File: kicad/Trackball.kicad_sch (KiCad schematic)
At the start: 40 parts, among them J1 Conn_01x04, J2 Conn_02x10_Odd_Even, SW1 SW_Push, SW2 SW_Push, U1 TCR2EF19, U2 PMW3360, U3 RP2040, U4 TLV73333PDBV, U5 W25Q128JVS, Y1 Crystal_GND24

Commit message: up
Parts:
- removed C1, C17, C2, C3, C4, C5, C6, C7, C8, C9: 100n, Capacitor_SMD:C_0402_1005Metric, symbol Device:C_Small
- removed C10, C13: 1u, Capacitor_SMD:C_0402_1005Metric, symbol Device:C_Small
- removed C18, C19: 30p, Capacitor_SMD:C_0402_1005Metric, symbol Device:C_Small
- removed J2: Conn_02x10_Odd_Even, Connector_PinHeader_2.54mm:PinHeader_2x10_P2.54mm_Vertical, symbol Connector_Generic:Conn_02x10_Odd_Even
- removed R3, R4: 27, Resistor_SMD:R_0402_1005Metric, symbol Device:R_Small
- removed R5: 10k, Resistor_SMD:R_0402_1005Metric, symbol Device:R_Small
- removed R6, R7: 1k, Resistor_SMD:R_0402_1005Metric, symbol Device:R_Small
- removed SW1, SW2: SW_Push, Button_Switch_SMD:SW_SPST_Omron_B3FS-100xP, symbol Switch:SW_Push
- removed U3: RP2040, RP2040:RP2040-QFN-56, symbol RP2040:RP2040
- removed U5: W25Q128JVS, Package_SO:SOIC-8_5.23x5.23mm_P1.27mm, symbol Trackball-rescue:W25Q128JVS-Memory_Flash
- removed Y1: Crystal_GND24, Crystal:Crystal_SMD_3225-4Pin_3.2x2.5mm, symbol Device:Crystal_GND24
- added C101, C102, C108, C110: 0.1u, Capacitor_SMD:C_0805_2012Metric, symbol Device:C_Small
- added C109, C111: 1u, Capacitor_SMD:C_0805_2012Metric, symbol Device:C_Small
- added J101: Conn_02x03_Counter_Clockwise, Connector_Harwin:Harwin_Gecko-G125-FVX0605L0X_2x03_P1.25mm_Vertical, symbol Connector_Generic:Conn_02x03_Counter_Clockwise
- added R103, R104: 10k, Resistor_SMD:R_0805_2012Metric, symbol Device:R_Small
- added SW1, SW2: Push_Button, PCM_Switch_Keyboard_Hotswap_Kailh:SW_Hotswap_Kailh_Choc_V1V2_1.00u, symbol PCM_SL_Devices:Push_Button
- added SW102: Push_Button, PCM_4ms_Switch:Switch_Toggle_SPDT_SubMini, symbol Switch:SW_Wuerth_450301014042
- added SW103, SW106: Push_Button, Button_Switch_SMD:SW_Push_1P1T_NO_CK_KSC7xxJ, symbol PCM_SL_Devices:Push_Button
- added SW3: RotaryEncoder_Switch_MP, PMW3360:RollerEncoder_Panasonic_EVQWGD001, symbol Device:RotaryEncoder_Switch_MP
- added U7: ESP32-S3-WROOM-2, PCM_Espressif:ESP32-S3-WROOM-2, symbol PCM_Espressif:ESP32-S3-WROOM-2
- C103: renamed from C15; footprint Capacitor_SMD:C_0402_1005Metric -> Capacitor_SMD:C_0805_2012Metric
- C104: renamed from C14; footprint Capacitor_SMD:C_0402_1005Metric -> Capacitor_SMD:C_0805_2012Metric
- C105: renamed from C16; footprint Capacitor_SMD:C_0402_1005Metric -> Capacitor_SMD:C_0805_2012Metric
- C106: renamed from C11; footprint Capacitor_SMD:C_0603_1608Metric -> Capacitor_SMD:C_0805_2012Metric
- C107: renamed from C12; footprint Capacitor_SMD:C_0603_1608Metric -> Capacitor_SMD:C_0805_2012Metric
- R101: renamed from R1; footprint Resistor_SMD:R_0402_1005Metric -> Resistor_SMD:R_0805_2012Metric
- R102: renamed from R2; footprint Resistor_SMD:R_0402_1005Metric -> Resistor_SMD:R_0805_2012Metric
- renumbered U1 to U103
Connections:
- net +3V3: now also J101.6 (Pin_6), R103.1, R104.1, SW102.2 (C), U7.2 (3V3)
- net +5V: now also SW102.3 (A); no longer C106.2, U103.1 (IN), U103.3 (EN)
- net D+: now also U7.14 (GPIO20/U1CTS/ADC2_CH9/CLK_OUT1/USB_D+)
- net D-: now also U7.13 (GPIO19/U1RTS/ADC2_CH8/CLK_OUT2/USB_D-)
- net GND: now also C101.2, C102.1, C108.1, C109.2, C110.1, C111.2, J101.5 (Pin_5), SW1.1, SW103.2, SW106.2, SW2.1, SW3.C, SW3.MP, SW3.S2, U7.1 (GND), U7.40 (GND), U7.41 (GND)
- net GPIO16: now also U7.9 (GPIO16/U0CTS/ADC2_CH5/XTAL_32K_N)
- net GPIO17: now also U7.10 (GPIO17/U1TXD/ADC2_CH6)
- net GPIO18: now also U7.11 (GPIO18/U1RXD/ADC2_CH7/CLK_OUT3)
- net MISO: now also U7.34 (MTDI/GPIO41/CLK_OUT1)
- net MOSI: now also U7.33 (MTDO/GPIO40/CLK_OUT2)
- net MOTION: now also U7.38 (GPIO2/TOUCH2/ADC1_CH1)
- net NCS: now also U7.35 (MTMS/GPIO42)
- net SCLK: now also U7.32 (MTCK/GPIO39/CLK_OUT3/SUBSPICS1)
- new net: C106.2, SW102.1 (B), U103.1 (IN), U103.3 (EN)
- new net EN: C108.2, C109.1, J101.1 (Pin_1), R103.2, SW103.1, U7.3 (EN)
- new net GPIO0: C110.2, C111.1, J101.4 (Pin_4), R104.2, SW106.1, U7.27 (GPIO0/BOOT)
- new net GPIO09: C102.2, SW3.B, U7.17 (GPIO9/TOUCH9/ADC1_CH8/FSPIHD/SUBSPIHD)
- new net GPIO10: C101.1, SW3.A, U7.18 (GPIO10/TOUCH10/ADC1_CH9/FSPICS0/FSPIIO4/SUBSPICS0)
- new net GPIO3: SW2.2, U7.15 (GPIO3/TOUCH3/ADC1_CH2)
- new net GPIO38: SW3.S1, U7.31 (GPIO38/FSPIWP/SUBSPIWP)
- new net GPIO46: SW1.2, U7.16 (GPIO46)
- new net RX: J101.3 (Pin_3), U7.36 (U0RXD/GPIO44/CLK_OUT2)
- new net TX: J101.2 (Pin_2), U7.37 (U0TXD/GPIO43/CLK_OUT1)
- no-connect marks 3 -> 1
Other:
- note removed: "Crystal"
- note removed: "Flash"
- note removed: "GPIO"

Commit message: update
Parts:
- added Brd101: SSD1306, SSD1306:128x64OLED, symbol SSD1306-128x64_OLED:SSD1306
- added D101, D102: LED_3mm, LED_THT:LED_D3.0mm, symbol PCM_SL_Devices:LED_3mm
- added R105, R106: R_1206, PCM_4ms_Resistor:R_0805_2012Metric, symbol PCM_Resistor_AKL:R_1206
- added SW101, SW104: Push_Button, PCM_openinput:SW_Micro_Switch, symbol PCM_SL_Devices:Push_Button
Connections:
- net +3V3: now also Brd101.2 (VCC)
- net GND: now also Brd101.1 (GND), D101.1, D102.1, SW101.1, SW104.1
- net GPIO25: now also SW1.2, U7.25 (GPIO48/SPICLK_N/SUBSPICLK_N_DIFF), SW101.2
- net GPIO3: now also R106.2; no longer SW2.2
- net GPIO38: now also R105.2; no longer SW3.S1
- net GPIO46: now also SW2.2, SW104.2; no longer SW1.2
- net MISO: now also U7.33 (MTDO/GPIO40/CLK_OUT2); no longer U7.34 (MTDI/GPIO41/CLK_OUT1)
- net MOSI: now also U7.34 (MTDI/GPIO41/CLK_OUT1); no longer U7.33 (MTDO/GPIO40/CLK_OUT2)
- net NCS: now also U7.32 (MTCK/GPIO39/CLK_OUT3/SUBSPICS1); no longer U7.35 (MTMS/GPIO42)
- net SCLK: now also U7.35 (MTMS/GPIO42); no longer U7.32 (MTCK/GPIO39/CLK_OUT3/SUBSPICS1)
- net GPIO11: now reaches U7.19 (GPIO11/TOUCH11/ADC2_CH0/FSPID/FSPIIO5/SUBSPID)
- net GPIO11: now also Brd101.4 (SDA)
- net GPIO12: now reaches U7.20 (GPIO12/TOUCH12/ADC2_CH1/FSPICLK/FSPIIO6/SUBSPICLK)
- net GPIO12: now also Brd101.3 (SCL)
- net GPIO13: now reaches U7.21 (GPIO13/TOUCH13/ADC2_CH2/FSPIQ/FSPIIO7/SUBSPIQ)
- net GPIO14: now reaches U7.22 (GPIO14/TOUCH14/ADC2_CH3/FSPIWP/FSPIDQS/SUBSPIWP)
- net GPIO14: now also SW3.S1
- net GPIO21: now reaches U7.23 (GPIO21)
- net GPIO21: now also C101.1, SW3.A
- net GPIO37: now reaches U7.24 (GPIO47/SPICLK_P/SUBSPICLK_P_DIFF)
- net GPIO37: now also C102.2, SW3.B
- removed net GPIO09: C102.2, SW3.B, U7.17 (GPIO9/TOUCH9/ADC1_CH8/FSPIHD/SUBSPIHD)
- removed net GPIO10: C101.1, SW3.A, U7.18 (GPIO10/TOUCH10/ADC1_CH9/FSPICS0/FSPIIO4/SUBSPICS0)
- new net: D101.2, R105.1
- new net: D102.2, R106.1
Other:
- moved on the sheet: SW2

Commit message: V1 prebuild
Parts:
- added J2: Conn_02x04_Counter_Clockwise, Connector_IDC:IDC-Header_2x04_P2.54mm_Vertical, symbol Connector_Generic:Conn_02x04_Counter_Clockwise
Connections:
- net +3V3: now also J2.2 (Pin_2)
- net GND: now also J2.1 (Pin_1)
- net GPIO13: now also J2.3 (Pin_3)
- net GPIO18: now also J2.6 (Pin_6)
- net GPIO8: now reaches U7.12 (GPIO8/TOUCH8/ADC1_CH7/SUBSPICS1)
- net GPIO8: now also J2.4 (Pin_4)
- net GPIO9: now reaches U7.17 (GPIO9/TOUCH9/ADC1_CH8/FSPIHD/SUBSPIHD)
- net GPIO9: now also J2.8 (Pin_8)
- net GPIO10: now reaches U7.18 (GPIO10/TOUCH10/ADC1_CH9/FSPICS0/FSPIIO4/SUBSPICS0)
- net GPIO10: now also J2.5 (Pin_5)
- net GPIO45: now reaches U7.26 (GPIO45)
- net GPIO45: now also J2.7 (Pin_7)

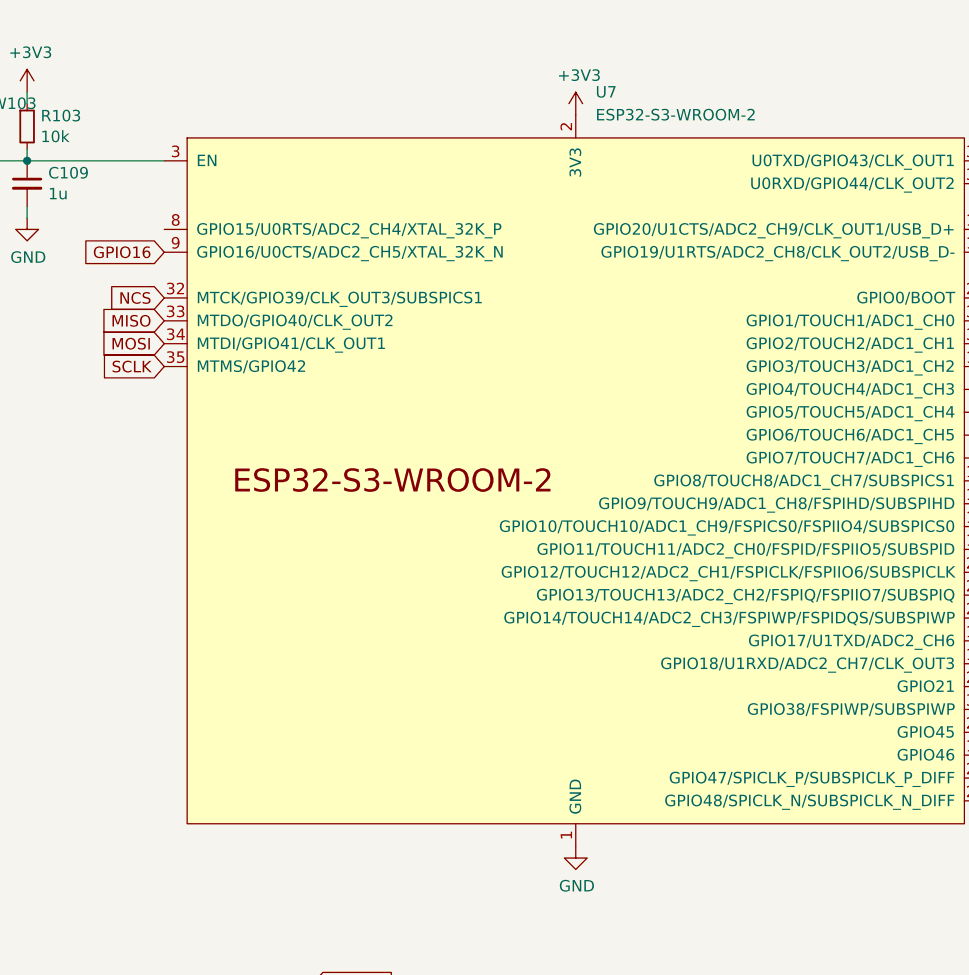
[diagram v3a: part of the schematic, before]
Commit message: changement wroom 2 a 1
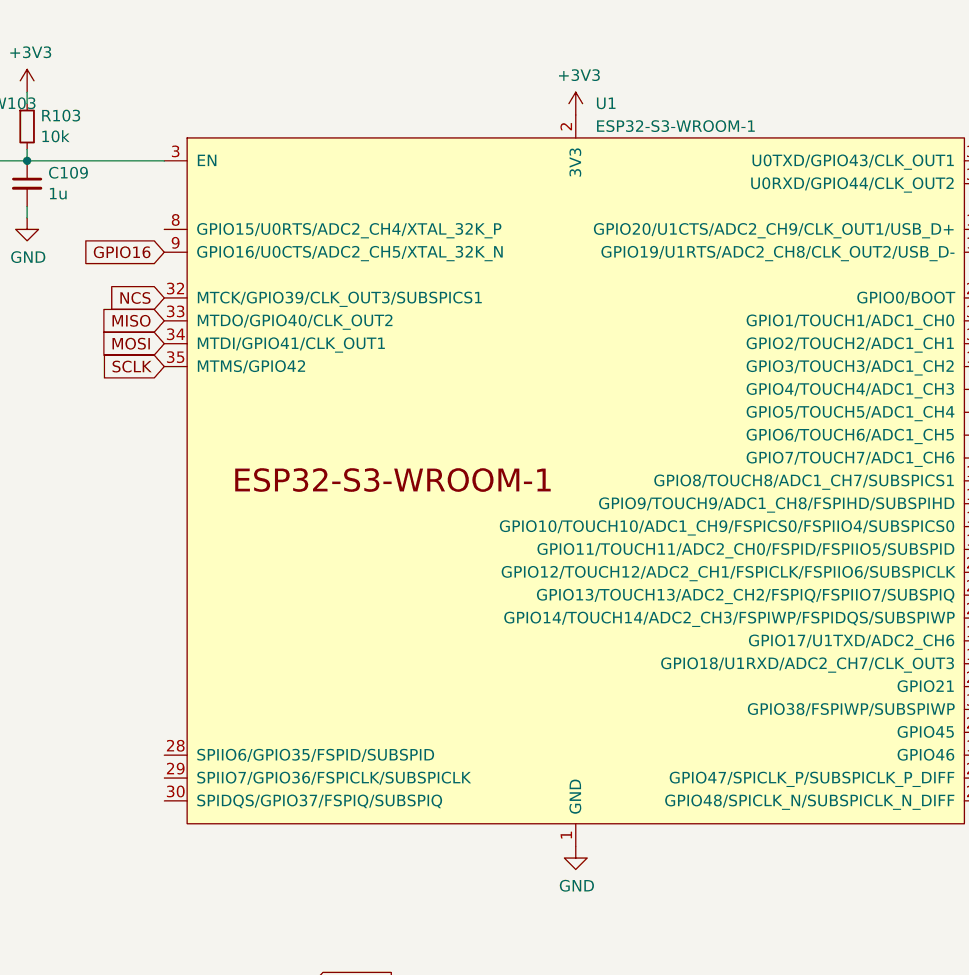
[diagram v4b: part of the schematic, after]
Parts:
- removed U7: ESP32-S3-WROOM-2, PCM_Espressif:ESP32-S3-WROOM-2, symbol PCM_Espressif:ESP32-S3-WROOM-2
- added U1: ESP32-S3-WROOM-1, PCM_Espressif:ESP32-S3-WROOM-1, symbol PCM_Espressif:ESP32-S3-WROOM-1
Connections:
- net +3V3: now also U1.2 (3V3)
- net D+: now also U1.14 (GPIO20/U1CTS/ADC2_CH9/CLK_OUT1/USB_D+)
- net D-: now also U1.13 (GPIO19/U1RTS/ADC2_CH8/CLK_OUT2/USB_D-)
- net EN: now also U1.3 (EN)
- net GND: now also U1.1 (GND), U1.40 (GND), U1.41 (GND)
- net GPIO0: now also U1.27 (GPIO0/BOOT)
- net GPIO10: now also U1.18 (GPIO10/TOUCH10/ADC1_CH9/FSPICS0/FSPIIO4/SUBSPICS0)
- net GPIO11: now also U1.19 (GPIO11/TOUCH11/ADC2_CH0/FSPID/FSPIIO5/SUBSPID)
- net GPIO12: now also U1.20 (GPIO12/TOUCH12/ADC2_CH1/FSPICLK/FSPIIO6/SUBSPICLK)
- net GPIO13: now also U1.21 (GPIO13/TOUCH13/ADC2_CH2/FSPIQ/FSPIIO7/SUBSPIQ)
- net GPIO14: now also U1.22 (GPIO14/TOUCH14/ADC2_CH3/FSPIWP/FSPIDQS/SUBSPIWP)
- net GPIO16: now also U1.9 (GPIO16/U0CTS/ADC2_CH5/XTAL_32K_N)
- net GPIO17: now also U1.10 (GPIO17/U1TXD/ADC2_CH6)
- net GPIO18: now also U1.11 (GPIO18/U1RXD/ADC2_CH7/CLK_OUT3)
- net GPIO21: now also U1.23 (GPIO21)
- net GPIO25: now also U1.25 (GPIO48/SPICLK_N/SUBSPICLK_N_DIFF)
- net GPIO3: now also U1.15 (GPIO3/TOUCH3/ADC1_CH2)
- net GPIO37: now also U1.24 (GPIO47/SPICLK_P/SUBSPICLK_P_DIFF)
- net GPIO38: now also U1.31 (GPIO38/FSPIWP/SUBSPIWP)
- net GPIO45: now also U1.26 (GPIO45)
- net GPIO46: now also U1.16 (GPIO46)
- net GPIO8: now also U1.12 (GPIO8/TOUCH8/ADC1_CH7/SUBSPICS1)
- net GPIO9: now also U1.17 (GPIO9/TOUCH9/ADC1_CH8/FSPIHD/SUBSPIHD)
- net MISO: now also U1.33 (MTDO/GPIO40/CLK_OUT2)
- net MOSI: now also U1.34 (MTDI/GPIO41/CLK_OUT1)
- net MOTION: now also U1.38 (GPIO2/TOUCH2/ADC1_CH1)
- net NCS: now also U1.32 (MTCK/GPIO39/CLK_OUT3/SUBSPICS1)
- net RX: now also U1.36 (U0RXD/GPIO44/CLK_OUT2)
- net SCLK: now also U1.35 (MTMS/GPIO42)
- net TX: now also U1.37 (U0TXD/GPIO43/CLK_OUT1)
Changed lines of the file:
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@@
+	)
+	(symbol
+		(lib_id "PCM_Espressif:ESP32-S3-WROOM-1")
+		(at 231.14 64.77 0)
+		(unit 1)
+		(exclude_from_sim no)
+		(in_bom yes)
+		(on_board yes)
+		(dnp no)
+		(fields_autoplaced yes)
+		(property "Reference" "U1"
+			(at 233.3341 22.86 0)
+			(effects
+				(font
+					(size 1.27 1.27)
+				)
+				(justify left)
+			)
+		)
+		(property "Value" "ESP32-S3-WROOM-1"
+			(at 233.3341 25.4 0)
+			(effects
+				(font
+					(size 1.27 1.27)
+				)
+				(justify left)
+			)
+		)
+		(property "Footprint" "PCM_Espressif:ESP32-S3-WROOM-1"
+			(at 233.68 113.03 0)
+			(effects
+				(font
+					(size 1.27 1.27)
+				)
+				(hide yes)
+			)
+		)
+		(property "Datasheet" "https://www.espressif.com/sites/default/files/documentation/esp32-s3-wroom-1_wroom-1u_datasheet_en.pdf"
+			(at 233.68 115.57 0)
+			(effects
+				(font
+					(size 1.27 1.27)
+				)
+				(hide yes)
+			)
+		)
+		(property "Description" "2.4 GHz WiFi (802.11 b/g/n) and Bluetooth ® 5 (LE) module Built around ESP32S3 series of SoCs, Xtensa ® dualcore 32bit LX7 microprocessor Flash up to 16 MB, PSRAM up to 8 MB 36 GPIOs, rich set of peripherals Onboard PCB antenna"
+			(at 231.14 64.77 0)
+			(effects
+				(font
+					(size 1.27 1.27)
+				)
+				(hide yes)
+			)
+		)
+		(pin "4"
+		)
+		(pin "14"
+		)
+		(pin "3"
+		)
+		(pin "29"
+		)
+		(pin "35"
+		)
+		(pin "40"
+		)
+		(pin "33"
+		)
+		(pin "15"
+		)
+		(pin "18"
+		)
+		(pin "19"
+		)
+		(pin "20"
+		)
+		(pin "21"
+		)
+		(pin "17"
+		)
+		(pin "24"
+		)
+		(pin "11"
+		)
+		(pin "26"
+		)
+		(pin "30"
+		)
+		(pin "34"
+		)
+		(pin "27"
+		)
+		(pin "37"
+		)
+		(pin "39"
+		)
+		(pin "41"
+		)
+		(pin "6"
+		)
+		(pin "2"
+		)
+		(pin "12"
+		)
+		(pin "9"
+		)
+		(pin "5"
+		)
+		(pin "16"
+		)
+		(pin "8"
+		)
+		(pin "10"
+		)
+		(pin "38"
+		)
+		(pin "25"
+		)
+		(pin "7"
+		)
+		(pin "1"
+		)
+		(pin "32"
+		)
+		(pin "36"
+		)
+		(pin "13"
+		)
+		(pin "22"
+		)
+		(pin "28"
+		)
+		(pin "31"
+		)
+		(pin "23"
+		)
+		(instances
+			(project ""
+				(path "/0da53b0a-8f1e-4a10-82c1-3eecfed721ae"
+					(reference "U1")
+					(unit 1)
+				)
+			)
+		)
 	)
 	(symbol
@@
 					(unit 1)
 				)
-			)
-		)
-	)
-	(symbol
-		(lib_id "PCM_Espressif:ESP32-S3-WROOM-2")
-		(at 231.14 64.77 0)
-		(unit 1)
-		(exclude_from_sim no)
-		(in_bom yes)
-		(on_board yes)
-		(dnp no)
-		(fields_autoplaced yes)
-		(property "Reference" "U7"
-			(at 233.3341 21.59 0)
-			(effects
-				(font
-					(size 1.27 1.27)
-				)
-				(justify left)
-			)
-		)
-		(property "Value" "ESP32-S3-WROOM-2"
-			(at 233.3341 24.13 0)
-			(effects
-				(font
-					(size 1.27 1.27)
-				)
-				(justify left)
-			)
-		)
-		(property "Footprint" "PCM_Espressif:ESP32-S3-WROOM-2"
-			(at 233.68 113.03 0)
-			(effects
-				(font
-					(size 1.27 1.27)
-				)
-				(hide yes)
-			)
-		)
-		(property "Datasheet" "https://www.espressif.com/sites/default/files/documentation/esp32-s3-wroom-2_datasheet_en.pdf"
-			(at 233.68 115.57 0)
-			(effects
-				(font
-					(size 1.27 1.27)
-				)
-				(hide yes)
-			)
-		)
-		(property "Description" "2.4 GHz WiFi (802.11 b/g/n) and Bluetooth ® 5 (LE) module Built around ESP32S3 series of SoCs, Xtensa ® dualcore 32bit LX7 microprocessor Flash up to 16 MB, PSRAM up to 8 MB 36 GPIOs, rich set of peripherals Onboard PCB antenna"
-			(at 231.14 64.77 0)
-			(effects
-				(font
-					(size 1.27 1.27)
-				)
-				(hide yes)
-			)
-		)
-		(pin "4"
-		)
-		(pin "5"
-		)
-		(pin "41"
-		)
-		(pin "2"
-		)
-		(pin "32"
-		)
-		(pin "17"
-		)
-		(pin "11"
-		)
-		(pin "23"
-		)
-		(pin "12"
-		)
-		(pin "25"
-		)
-		(pin "1"
-		)
-		(pin "27"
-		)
-		(pin "31"
-		)
-		(pin "33"
-		)
-		(pin "30"
-		)
-		(pin "36"
-		)
-		(pin "37"
-		)
-		(pin "38"
-		)
-		(pin "8"
-		)
-		(pin "10"
-		)
-		(pin "15"
-		)
-		(pin "34"
-		)
-		(pin "19"
-		)
-		(pin "6"
-		)
-		(pin "24"
-		)
-		(pin "39"
-		)
-		(pin "22"
-		)
-		(pin "18"
-		)
-		(pin "21"
-		)
-		(pin "29"
-		)
-		(pin "3"
-		)
-		(pin "28"
-		)
-		(pin "35"
-		)
-		(pin "16"
-		)
-		(pin "9"
-		)
-		(pin "20"
-		)
-		(pin "13"
-		)
-		(pin "14"
-		)
-		(pin "26"
-		)
-		(pin "40"
-		)
-		(pin "7"
-		)
-		(instances
-			(project ""
-				(path "/0da53b0a-8f1e-4a10-82c1-3eecfed721ae"
-					(reference "U7")
-					(unit 1)
-				)

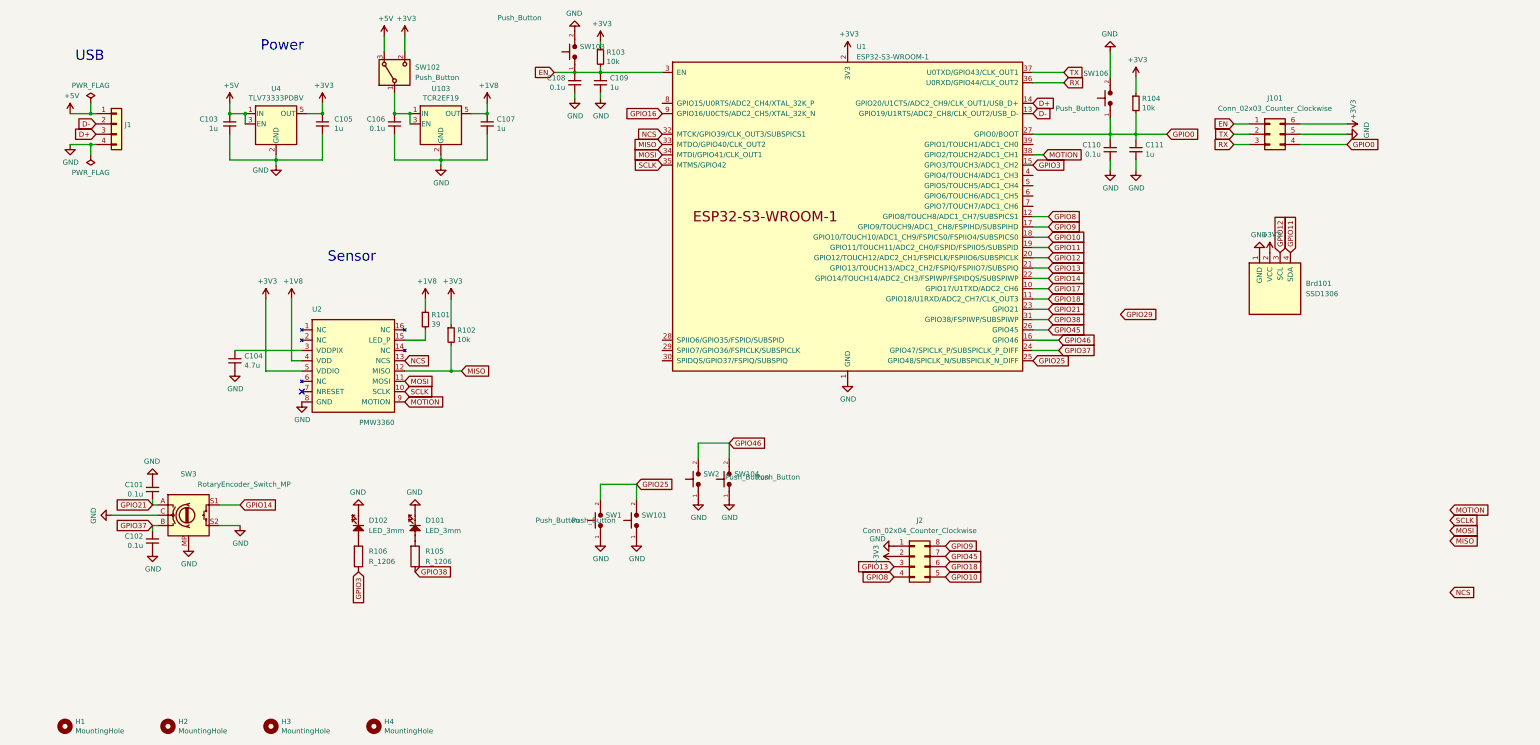
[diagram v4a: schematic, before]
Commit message: ajout test pad
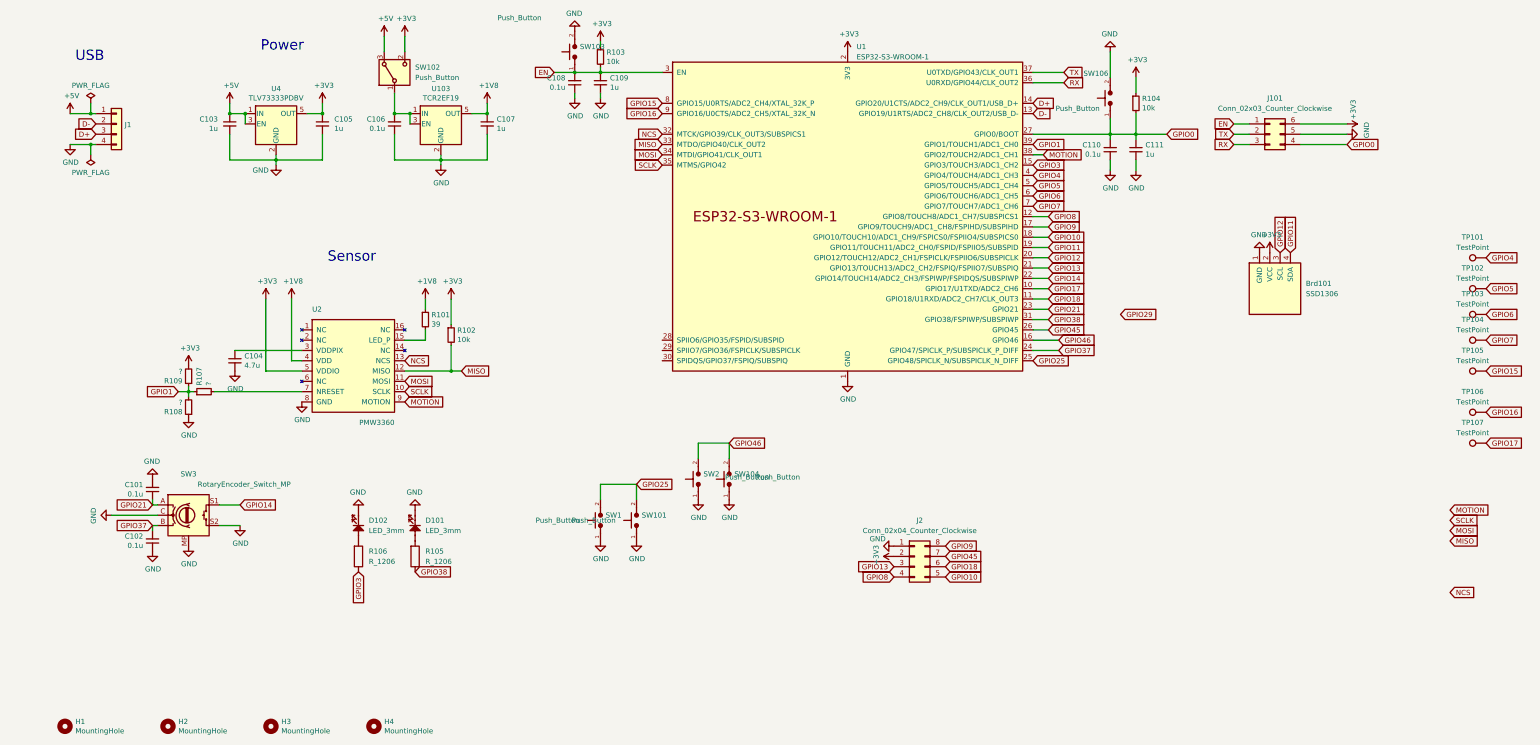
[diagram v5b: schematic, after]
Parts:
- added R107, R108, R109: ?, Resistor_SMD:R_0805_2012Metric, symbol Device:R_Small
- added TP101, TP102, TP103, TP104, TP105, TP106, TP107: TestPoint, TestPoint:TestPoint_Pad_D1.0mm, symbol Connector:TestPoint
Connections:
- net +3V3: now also R109.2
- net GND: now also R108.1
- net GPIO16: now also TP106.1
- net GPIO17: now also TP107.1
- net at U2.7 (NRESET): now also R107.2
- net GPIO1: now reaches U1.39 (GPIO1/TOUCH1/ADC1_CH0)
- net GPIO1: now also R107.1, R108.2, R109.1
- net GPIO4: now reaches U1.4 (GPIO4/TOUCH4/ADC1_CH3)
- net GPIO4: now also TP101.1
- net GPIO5: now reaches U1.5 (GPIO5/TOUCH5/ADC1_CH4)
- net GPIO5: now also TP102.1
- net GPIO6: now reaches U1.6 (GPIO6/TOUCH6/ADC1_CH5)
- net GPIO6: now also TP103.1
- net GPIO7: now reaches U1.7 (GPIO7/TOUCH7/ADC1_CH6)
- net GPIO7: now also TP104.1
- net GPIO15: now reaches U1.8 (GPIO15/U0RTS/ADC2_CH4/XTAL_32K_P)
- net GPIO15: now also TP105.1
- no-connect marks 1 -> 0
